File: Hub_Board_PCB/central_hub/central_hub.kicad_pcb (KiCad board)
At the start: 2 copper layers, 0.7 x 1.7 mm, 90 parts, among them J1 CAN_OUT, J10 Conn_02x03_Counter_Clockwise, J2 Barrel_Jack_MountingPin, J3 Screw_Terminal_01x14, J4 Conn_02x05_Counter_Clockwise, J5 CSP-USC16-TR, J6 Screw_Terminal_01x08, J7 Conn_02x03_Counter_Clockwise, J8 Conn_01x02, J9 Screw_Terminal_01x04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

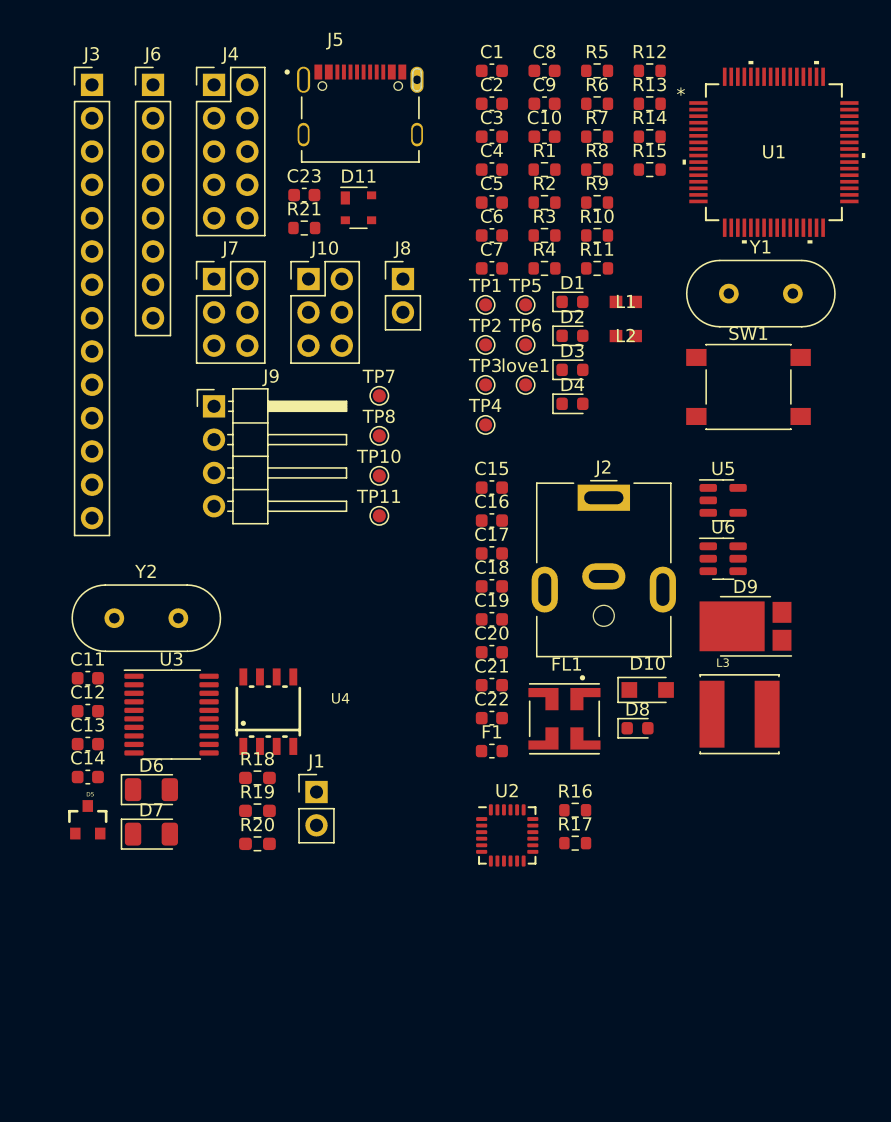
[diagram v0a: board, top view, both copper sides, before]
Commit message: Fixed header sizes
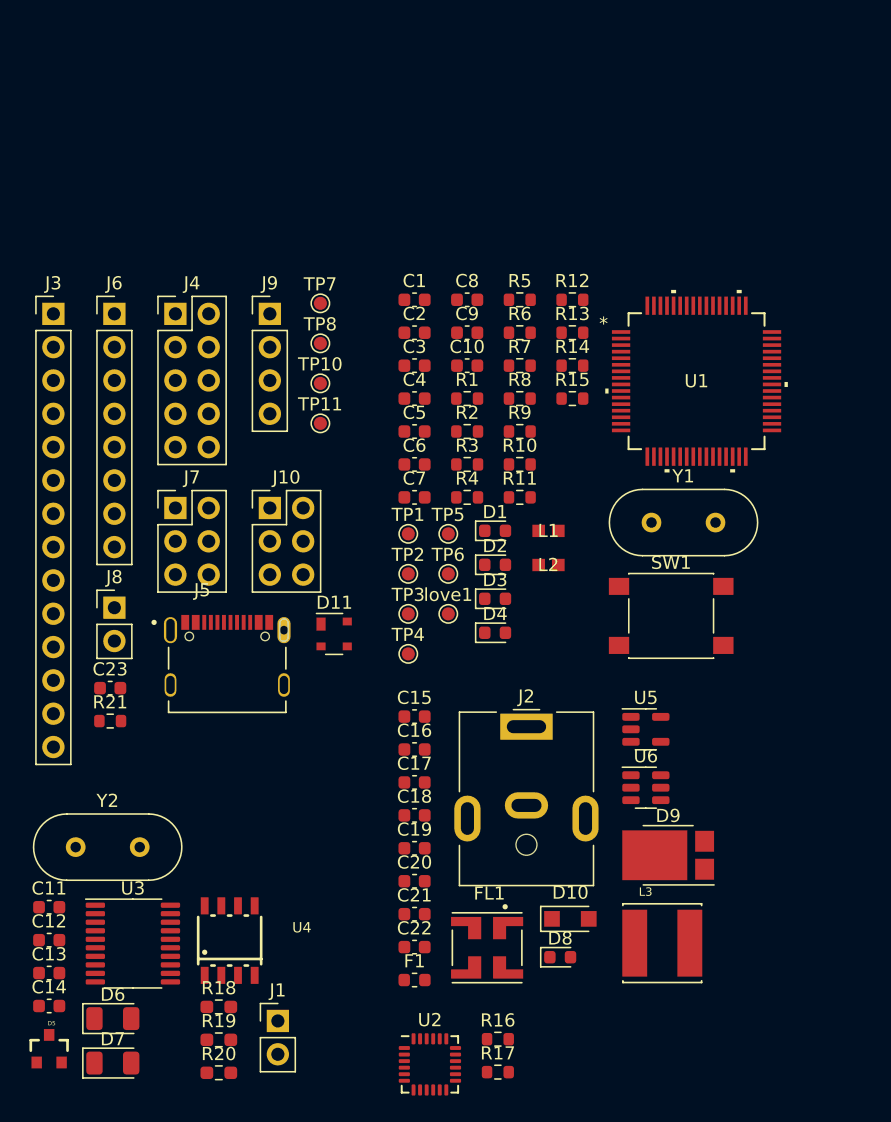
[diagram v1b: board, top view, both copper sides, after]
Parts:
- J9: footprint Connector_PinHeader_2.54mm:PinHeader_1x04_P2.54mm_Horizontal -> Connector_PinHeader_2.54mm:PinHeader_1x04_P2.54mm_Vertical
- moved J5 43.2 mm to (137.5, 97.5)
- moved C23 40.4 mm to (128.5, 102.5)
- moved R21 40.4 mm to (128.5, 105.0)
- moved J8 33.3 mm to (128.9, 96.3)
- moved D11 32.5 mm to (145.6, 98.3)
- moved R10 18.4 mm to (159.8, 85.4)
- moved TP4 18.4 mm to (151.3, 99.9)
- moved R6 18.4 mm to (159.8, 75.4)
- moved R7 18.4 mm to (159.8, 77.9)
- moved C15 18.4 mm to (151.7, 104.7)
- moved C18 18.4 mm to (151.7, 112.2)
- moved C6 18.4 mm to (151.7, 85.4)
- moved D4 18.4 mm to (157.9, 98.3)
- moved F1 18.4 mm to (151.7, 124.7)
- moved R16 18.4 mm to (158.1, 129.2)
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
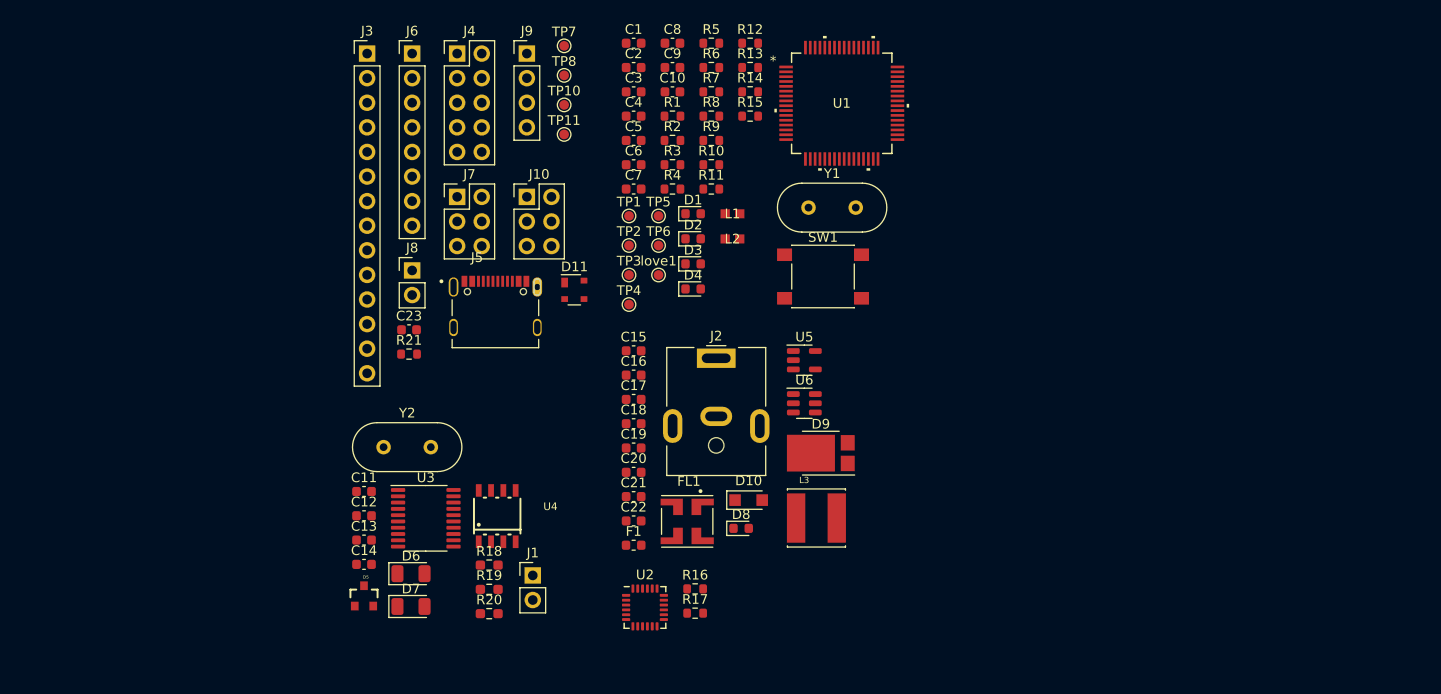
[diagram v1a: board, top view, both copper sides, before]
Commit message: Started Layout (hub board)
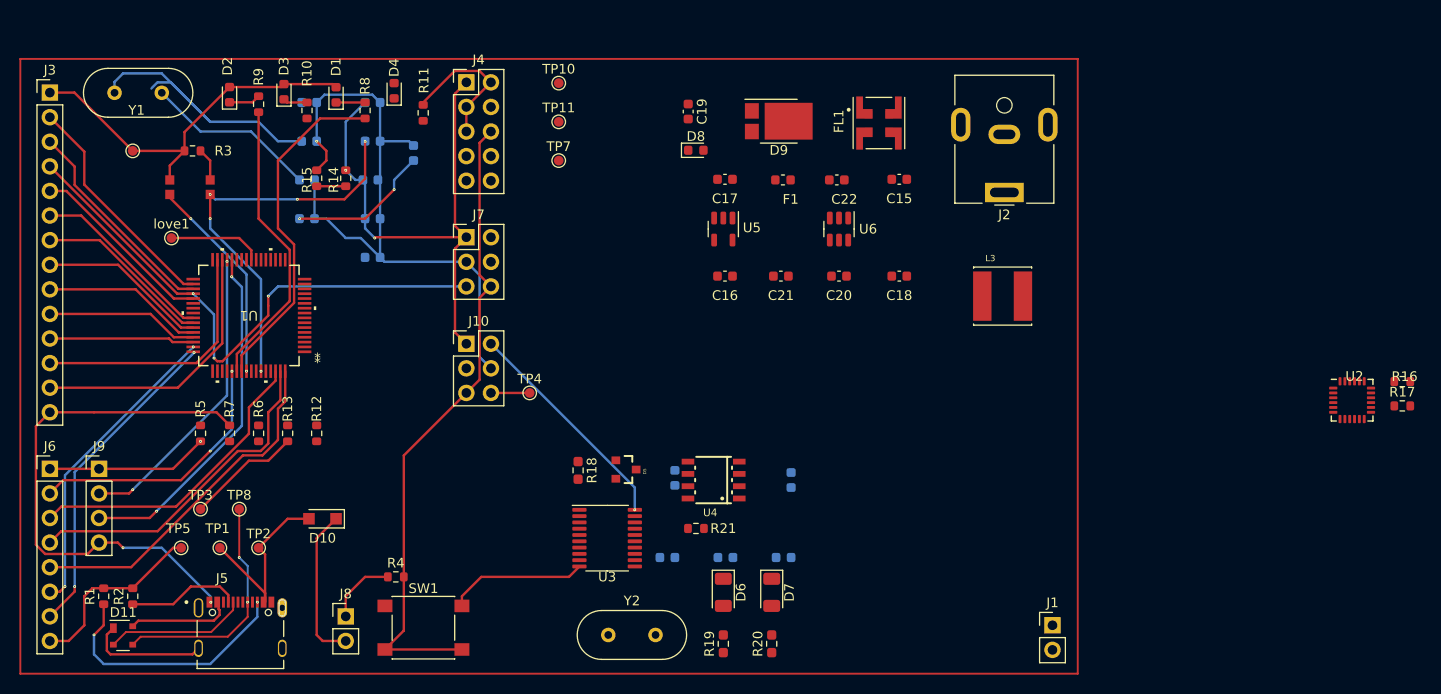
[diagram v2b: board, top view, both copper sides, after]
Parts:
- C1, C10, C11, C12, C13, C14, C2, C23, C3, C4, C5, C6, C7, C8, C9: moved to B.Cu
- moved R1 76.9 mm to (97.0, 130.0), turned to 90 degrees
- moved R16 76.1 mm to (231.1, 107.8)
- moved R17 76.1 mm to (231.1, 110.3)
- moved U2 76.1 mm to (225.9, 109.8)
- moved R2 73.0 mm to (100.0, 130.0), turned to 90 degrees
- moved Y1 67.8 mm to (103.0, 78.0), turned to 180 degrees
- moved R5 66.4 mm to (107.0, 113.2), turned to 90 degrees
- moved U1 65.0 mm to (112.0, 101.0), turned to 180 degrees
- moved J9 61.6 mm to (96.5, 116.8)
- moved R7 61.0 mm to (110.0, 113.2), turned to 90 degrees
- moved R13 60.9 mm to (116.0, 113.2), turned to 90 degrees
- moved R12 60.2 mm to (119.0, 113.2), turned to 90 degrees
- moved R6 60.1 mm to (113.0, 113.2), turned to -90 degrees
- moved TP5 60.1 mm to (105.0, 125.0)
- moved D11 58.7 mm to (99.0, 134.1)
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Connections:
- J3 pad 10: D3 -> D4
- J3 pad 11: D2 -> D5
- J3 pad 12: D1 -> D0
- J3 pad 13: D0 -> D1
- J3 pad 2: D13 -> D11
- J3 pad 4: D11 -> D13
- J3 pad 8: D5 -> D2
- J3 pad 9: D4 -> D3
- J5 pad A5: /Connectors/CC1 -> CC1
- J5 pad B5: /Connectors/CC2 -> CC2
- J6 pad 3: A1 -> A3
- J6 pad 5: A3 -> A1
- R1 pad 1: /MCU/CC2 -> CC2
- R2 pad 1: /MCU/CC1 -> CC1
- U3 pad 14: CAN_SCK -> D13
- U3 pad 16: CAN_SI -> D11
- U3 pad 17: CAN_SO -> D12
- U3 pad 18: CAN_CS -> D10
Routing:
- net GND: track 0.00 -> 172.6 mm, vias 0 -> 3
- net IOREF: track 0.00 -> 154.7 mm, vias 0 -> 4
- net ~{RESET}: track 0.00 -> 67.0 mm
- net D13: track 0.00 -> 58.4 mm, vias 0 -> 3
- net Net-(U1-P010/AN005/VREFH0): track 0.00 -> 41.4 mm, vias 0 -> 5
- net A1: track 0.00 -> 36.4 mm
- net D8: track 0.00 -> 36.3 mm, vias 0 -> 2
- net /MCU/P012: track 0.00 -> 35.5 mm
- net A2: track 0.00 -> 34.8 mm
- net A5: track 0.00 -> 33.4 mm, vias 0 -> 2
- net A4: track 0.00 -> 32.0 mm, vias 0 -> 2
- net A3: track 0.00 -> 31.8 mm
- net Net-(U1-P213/GTIOC0A/XTAL): track 0.00 -> 31.7 mm
- net D9: track 0.00 -> 31.3 mm, vias 0 -> 2
- net /MCU/P013: track 0.00 -> 30.7 mm
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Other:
- board size 0.7 x 1.7 mm -> 0.6 x 1.7 mm

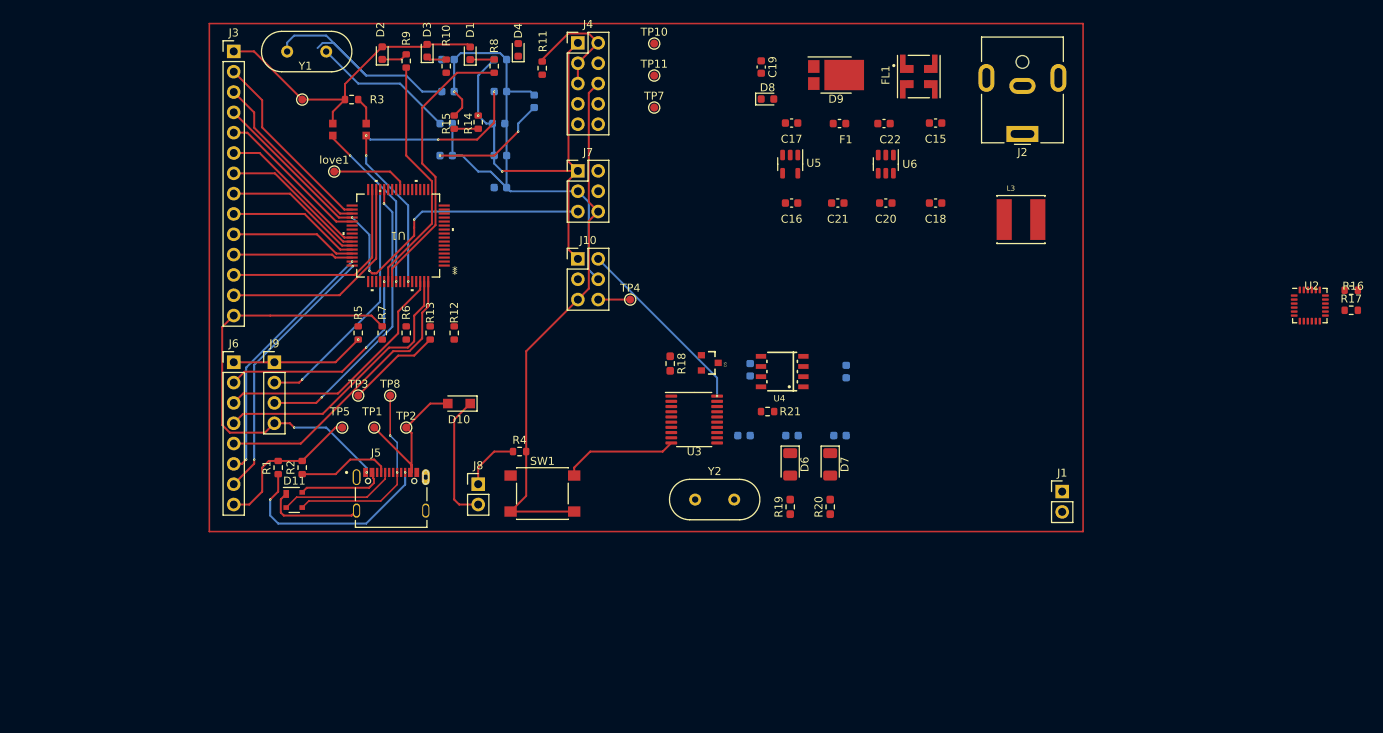
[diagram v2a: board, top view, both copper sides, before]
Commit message: Redid traces... might want auto trace lol
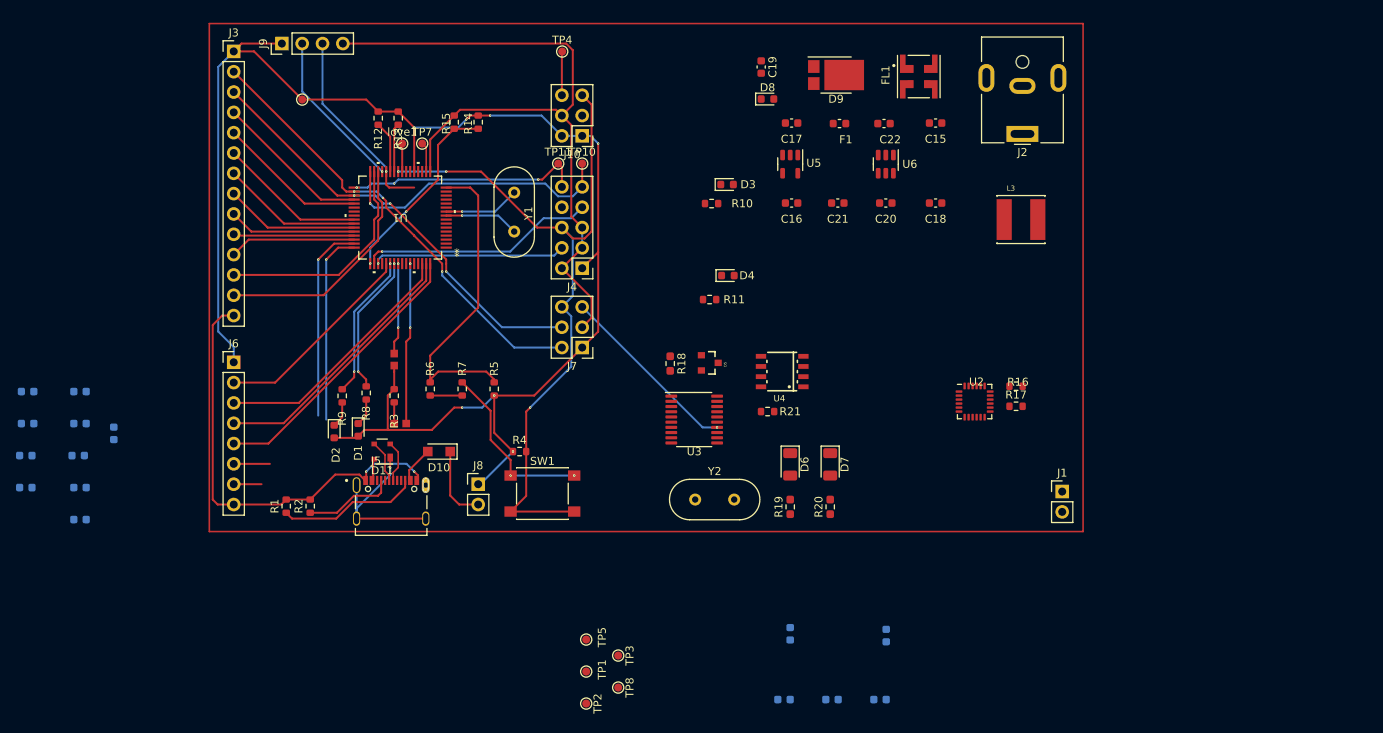
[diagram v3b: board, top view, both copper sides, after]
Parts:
- moved C1 67.0 mm to (72.2, 136.5)
- moved C4 67.0 mm to (72.2, 120.5)
- moved C5 67.0 mm to (72.2, 132.5)
- moved C8 67.0 mm to (72.2, 124.5)
- moved C10 67.0 mm to (65.7, 120.5)
- moved C2 67.0 mm to (65.7, 124.5)
- moved C3 67.0 mm to (65.5, 128.5)
- moved C6 67.0 mm to (72.0, 128.5)
- moved C7 67.0 mm to (76.5, 125.7)
- moved C9 67.0 mm to (65.5, 132.5)
- moved D1 49.1 mm to (107.0, 125.3), turned to -90 degrees
- moved D2 47.7 mm to (104.0, 125.5), turned to -90 degrees
- moved TP8 46.3 mm to (139.5, 157.5), turned to -90 degrees
- moved TP3 46.0 mm to (139.5, 153.5), turned to -90 degrees
- moved R8 43.9 mm to (108.0, 120.7), turned to 90 degrees
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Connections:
- U2 pad 1: unconnected-(U2-CLKIN-Pad1) -> GND
- U2 pad 10: unconnected-(U2-REGOUT-Pad10) -> GND
- U2 pad 11: unconnected-(U2-FSYNC-Pad11) -> GND
- U2 pad 20: unconnected-(U2-CPOUT-Pad20) -> GND
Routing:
- net Net-(U1-P407/USB_VBUS/ADTRG0): track 0.00 -> 39.8 mm
- net IOREF: track 154.7 -> 191.2 mm, vias 4 -> 7
- net P300: track 0.00 -> 36.0 mm, vias 0 -> 1
- net D11: track 23.9 -> 57.2 mm, vias 0 -> 3
- net D12: track 22.2 -> 54.1 mm, vias 0 -> 3
- net P108: track 0.00 -> 30.1 mm, vias 0 -> 3
- net P501: track 0.00 -> 29.5 mm, vias 0 -> 1
- net ~{RESET}: track 67.0 -> 93.7 mm, vias 0 -> 3
- net P502: track 0.00 -> 24.1 mm, vias 0 -> 1
- net VUSB: track 30.7 -> 7.29 mm
- net Net-(U1-P213/GTIOC0A/XTAL): track 31.7 -> 9.33 mm, vias 0 -> 1
- net Net-(U1-GTIOC2A/AN016/P500): track 3.00 -> 24.2 mm, vias 0 -> 2
- net Net-(U1-P010/AN005/VREFH0): track 41.4 -> 20.2 mm, vias 5 -> 2
- net USB_D+: track 24.5 -> 5.33 mm, vias 2 -> 0
- net /MCU/P012: track 35.5 -> 17.6 mm, vias 0 -> 2
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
